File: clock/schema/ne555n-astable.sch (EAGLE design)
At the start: 16 parts

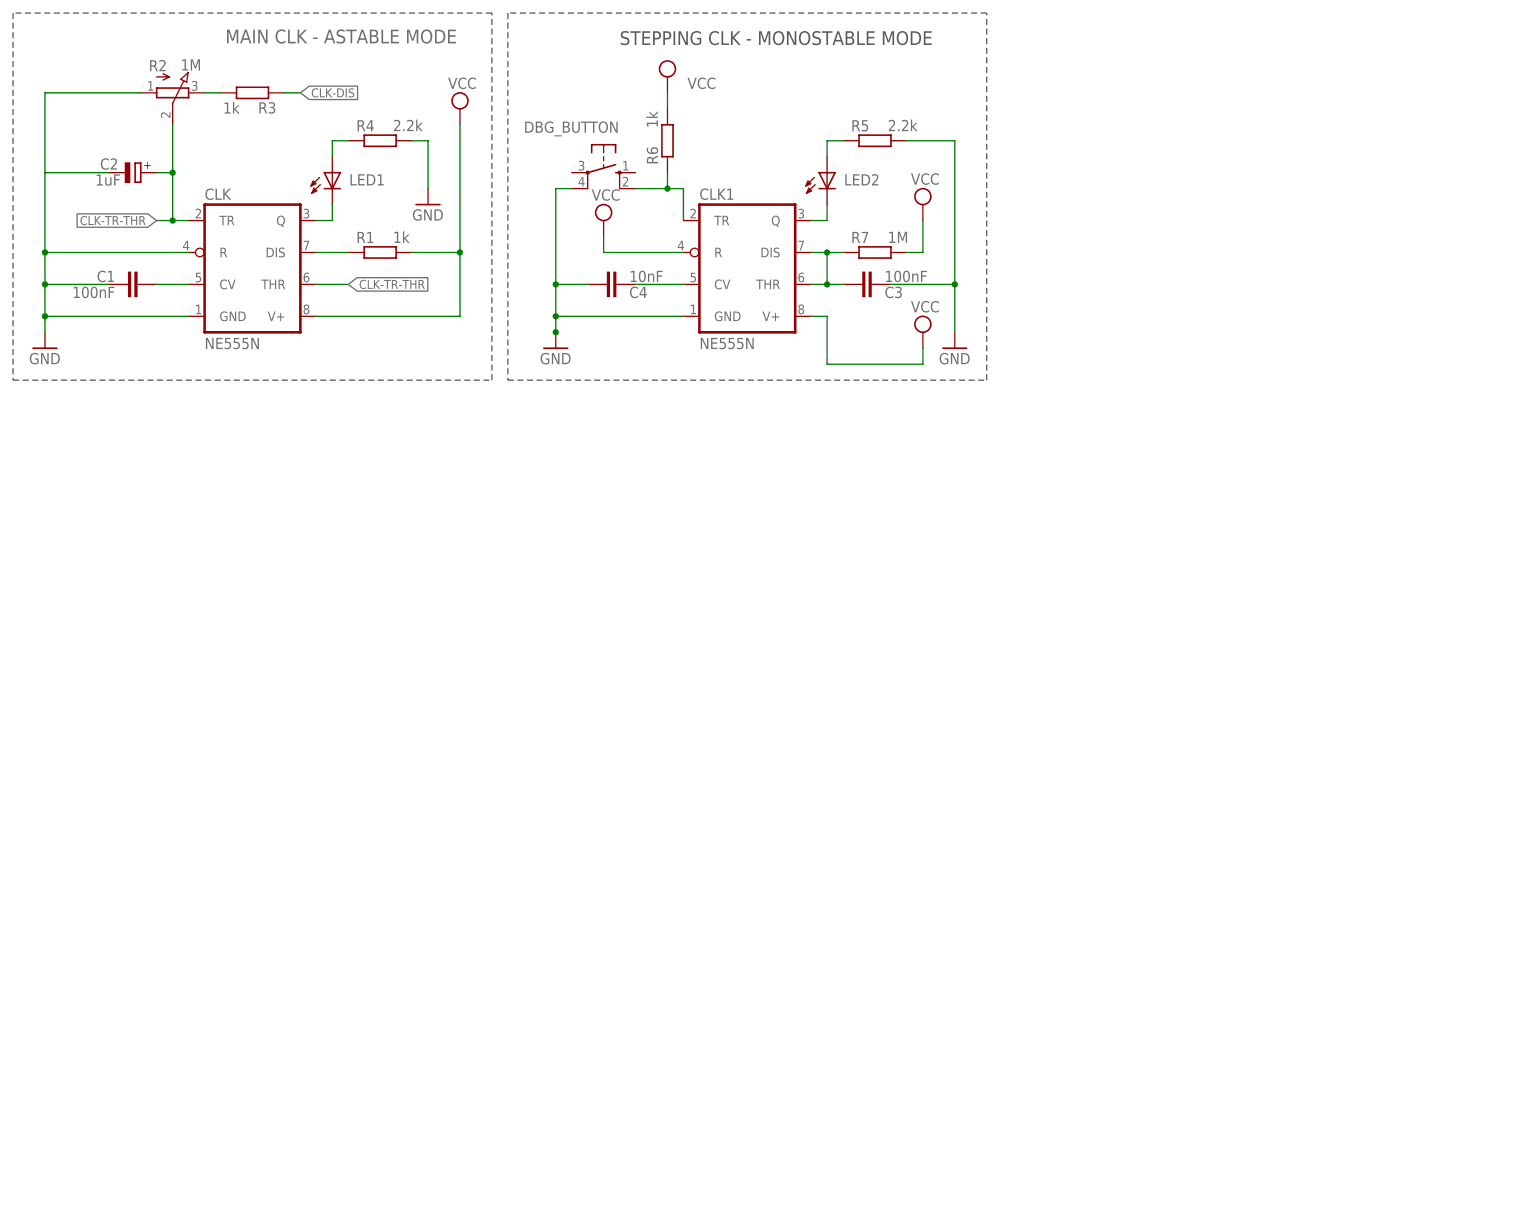
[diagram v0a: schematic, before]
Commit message: Splitted clock design and other related stuff from main directory
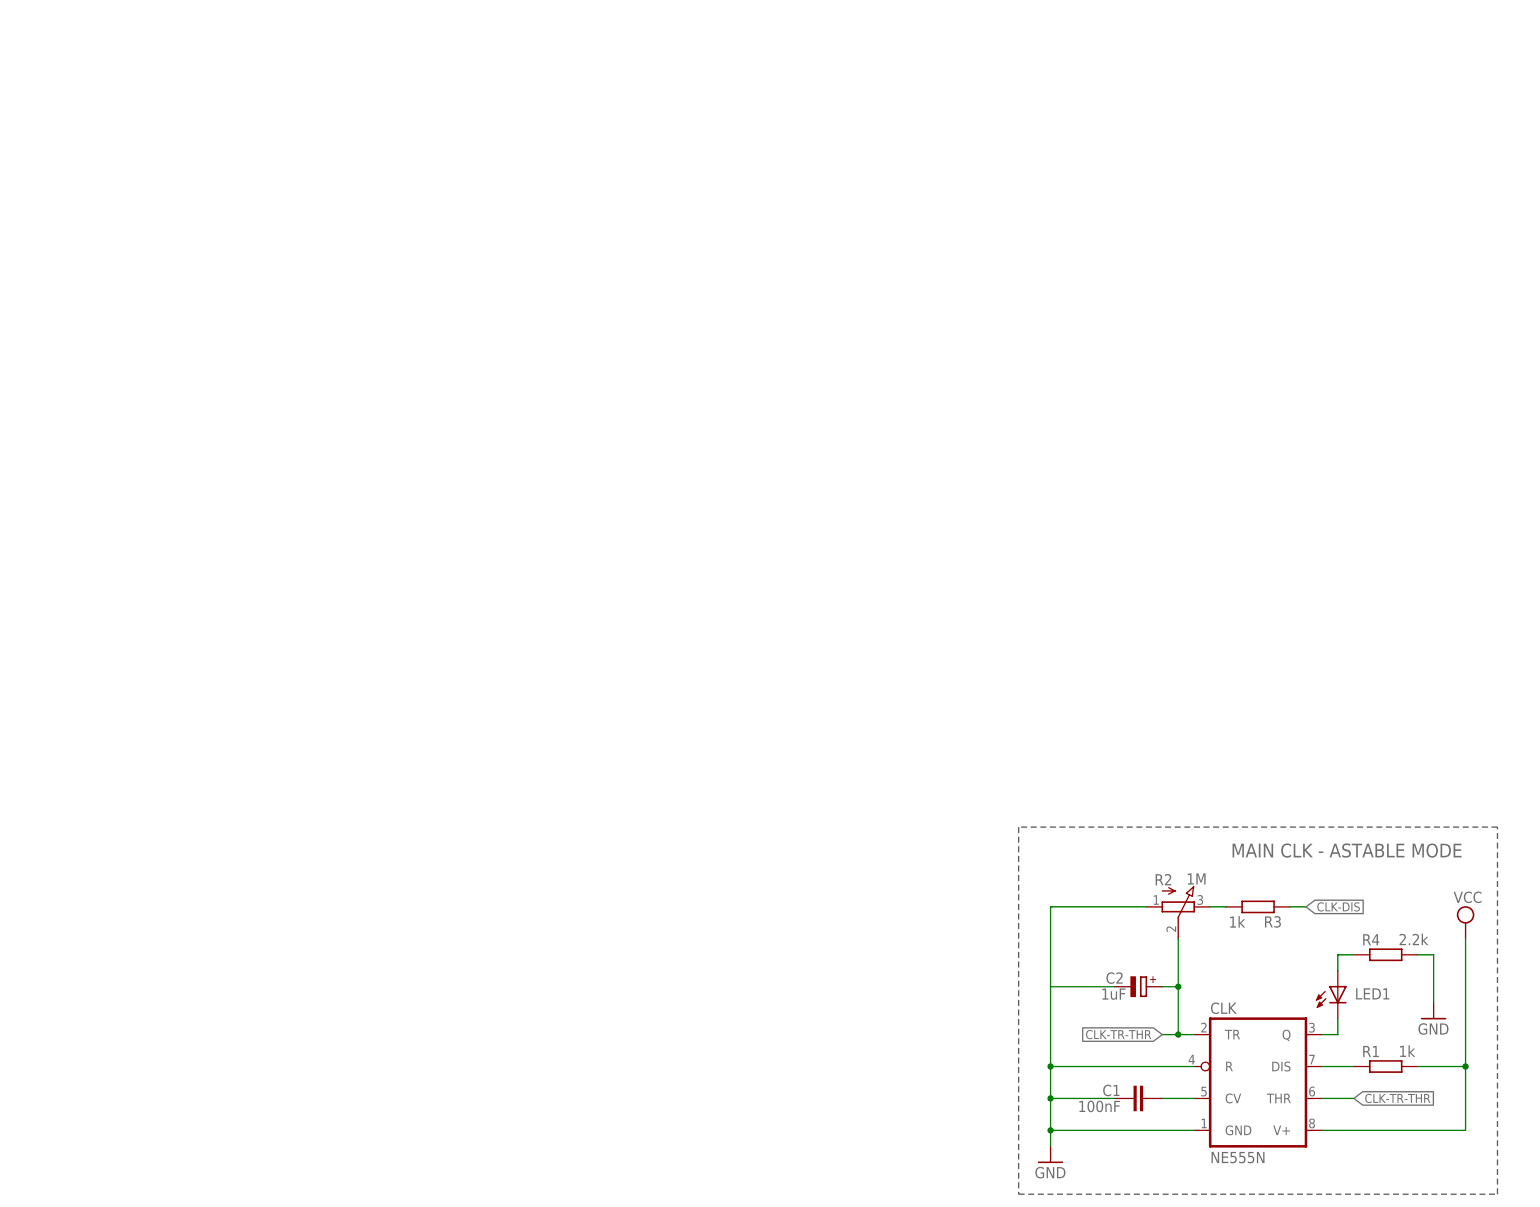
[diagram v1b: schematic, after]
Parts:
- removed C3: 100nF, resistor:C-EU025-050X050
- removed C4: 10nF, resistor:C-EU025-050X050
- removed CLK1: NE555N, linear:NE555N
- removed DBG_BUTTON: (no value), switch-omron:10-XX
- removed LED2: (no value), eagle-ltspice:LED_ELD260
- removed R5: 2.2k, resistor:R-EU_0204/5
- removed R6: 1k, resistor:R-EU_0204/5
- removed R7: 1M, resistor:R-EU_0204/5
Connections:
- removed net N$1: CLK1.Q, LED2.C
- removed net N$3: LED2.A, R5.1
- removed net N$5: CLK1.TR, DBG_BUTTON.S1, R6.1
- removed net N$6: C3.2, CLK1.DIS, CLK1.THR, R7.1
- removed net N$7: C4.1, CLK1.CV
- net GND: no longer C3.1, C4.2, CLK1.GND, DBG_BUTTON.P1, R5.2
- net VCC: no longer CLK1.R, CLK1.V+, R6.2, R7.2
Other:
- note removed: "STEPPING CLK - MONOSTABLE MODE"
- moved on the sheet: C1, C2, CLK, LED1, R1, R2, R3, R4
